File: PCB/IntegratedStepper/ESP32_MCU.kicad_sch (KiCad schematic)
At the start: 23 parts, among them Q1 SS8050-G, Q2 SS8050-G, U1 ESP32-WROOM-32E, U3 CP2102N-Axx-xQFN28

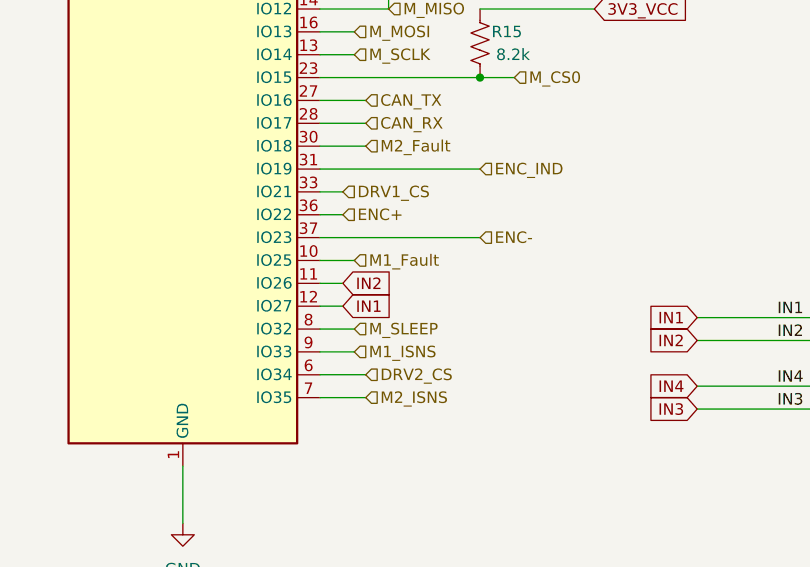
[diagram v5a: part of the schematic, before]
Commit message: update new layout with DRV8245
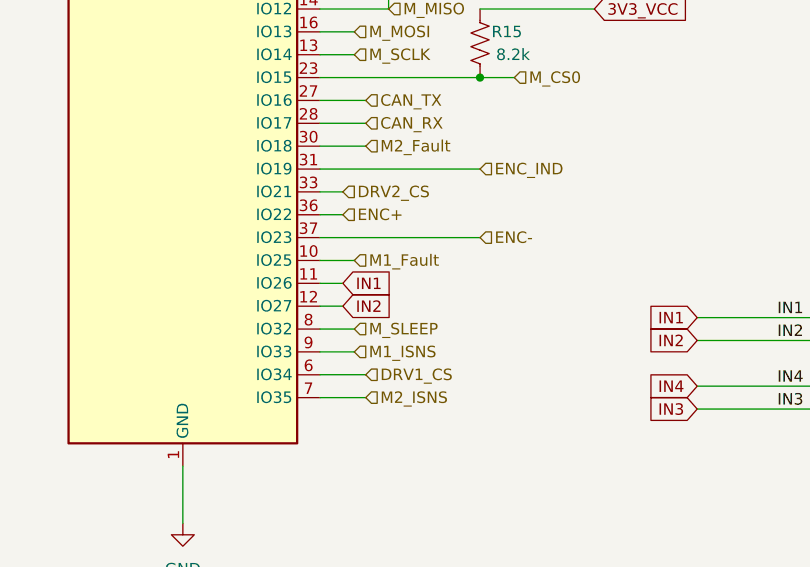
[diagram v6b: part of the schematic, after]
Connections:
- net DRV1_CS: now also U1.6 (IO34); no longer U1.33 (IO21)
- net DRV2_CS: now also U1.33 (IO21); no longer U1.6 (IO34)
- net IN1: now also U1.11 (IO26); no longer U1.12 (IO27)
- net IN2: now also U1.12 (IO27); no longer U1.11 (IO26)
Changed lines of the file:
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@@
+		)
+	)
+	(global_label "IN2"
+		(shape input)
+		(at 134.62 102.87 0)
+		(fields_autoplaced yes)
+		(effects
+			(font
+				(size 1.27 1.27)
+			)
+			(justify left)
+		)
+		(property "Intersheetrefs" "${INTERSHEET_REFS}"
+			(at 140.75 102.87 0)
+			(effects
+				(font
+					(size 1.27 1.27)
+				)
+				(justify left)
+				(hide yes)
+			)
 		)
 	)
@@
 		)
 	)
+	(global_label "IN1"
+		(shape input)
+		(at 134.62 100.33 0)
+		(fields_autoplaced yes)
+		(effects
+			(font
+				(size 1.27 1.27)
+			)
+			(justify left)
+		)
+		(property "Intersheetrefs" "${INTERSHEET_REFS}"
+			(at 140.75 100.33 0)
+			(effects
+				(font
+					(size 1.27 1.27)
+				)
+				(justify left)
+				(hide yes)
+			)
+		)
+	)
 	(global_label "EN"
 		(shape input)
@@
 		)
 	)
+	(global_label "RX"
+		(shape input)
+		(at 135.89 62.23 0)
+		(fields_autoplaced yes)
+		(effects
+			(font
+				(size 1.27 1.27)
+			)
+			(justify left)
+		)
+		(property "Intersheetrefs" "${INTERSHEET_REFS}"
+			(at 141.3547 62.23 0)
+			(effects
+				(font
+					(size 1.27 1.27)
+				)
+				(justify left)
+				(hide yes)
+			)
+		)
+	)
+	(global_label "DTR"
+		(shape input)
+		(at 36.83 147.32 180)
+		(fields_autoplaced yes)
+		(effects
+			(font
+				(size 1.27 1.27)
+			)
+			(justify right)
+		)
+		(property "Intersheetrefs" "${INTERSHEET_REFS}"
+			(at 30.3372 147.32 0)
+			(effects
+				(font
+					(size 1.27 1.27)
+				)
+				(justify right)
+				(hide yes)
+			)
+		)
+	)
+	(global_label "IN3"
+		(shape input)
+		(at 173.99 114.3 180)
+		(fields_autoplaced yes)
+		(effects
+			(font
+				(size 1.27 1.27)
+			)
+			(justify right)
+		)
+		(property "Intersheetrefs" "${INTERSHEET_REFS}"
+			(at 167.86 114.3 0)
+			(effects
+				(font
+					(size 1.27 1.27)
+				)
+				(justify right)
+				(hide yes)
+			)
+		)
+	)
 	(global_label "IN1"
 		(shape input)
-		(at 134.62 102.87 0)
-		(fields_autoplaced yes)
-		(effects
-			(font
-				(size 1.27 1.27)
-			)
-			(justify left)
-		)
-		(property "Intersheetrefs" "${INTERSHEET_REFS}"
-			(at 140.75 102.87 0)
-			(effects
-				(font
-					(size 1.27 1.27)
-				)
-				(justify left)
-				(hide yes)
-			)
-		)
-	)
-	(global_label "RX"
-		(shape input)
-		(at 135.89 62.23 0)
-		(fields_autoplaced yes)
-		(effects
-			(font
-				(size 1.27 1.27)
-			)
-			(justify left)
-		)
-		(property "Intersheetrefs" "${INTERSHEET_REFS}"
-			(at 141.3547 62.23 0)
-			(effects
-				(font
-					(size 1.27 1.27)
-				)
-				(justify left)
-				(hide yes)
-			)
-		)
-	)
-	(global_label "DTR"
-		(shape input)
-		(at 36.83 147.32 180)
-		(fields_autoplaced yes)
-		(effects
-			(font
-				(size 1.27 1.27)
-			)
-			(justify right)
-		)
-		(property "Intersheetrefs" "${INTERSHEET_REFS}"
-			(at 30.3372 147.32 0)
-			(effects
-				(font
-					(size 1.27 1.27)
-				)
-				(justify right)
-				(hide yes)
-			)
-		)
-	)
-	(global_label "IN3"
-		(shape input)
-		(at 173.99 114.3 180)
-		(fields_autoplaced yes)
-		(effects
-			(font
-				(size 1.27 1.27)
-			)
-			(justify right)
-		)
-		(property "Intersheetrefs" "${INTERSHEET_REFS}"
-			(at 167.86 114.3 0)
-			(effects
-				(font
-					(size 1.27 1.27)
-				)
-				(justify right)
-				(hide yes)
-			)
-		)
-	)
-	(global_label "IN1"
-		(shape input)
 		(at 173.99 104.14 180)
 		(fields_autoplaced yes)
@@
 		)
 	)
-	(global_label "IN2"
-		(shape input)
-		(at 134.62 100.33 0)
-		(fields_autoplaced yes)
-		(effects
-			(font
-				(size 1.27 1.27)
-			)
-			(justify left)
-		)
-		(property "Intersheetrefs" "${INTERSHEET_REFS}"
-			(at 140.75 100.33 0)
-			(effects
-				(font
-					(size 1.27 1.27)
-				)
-				(justify left)
-				(hide yes)
-			)
-		)
-	)
 	(global_label "IN4"
 		(shape input)
@@
 		)
 	)
+	(hierarchical_label "DRV1_CS"
+		(shape input)
+		(at 137.16 110.49 0)
+		(fields_autoplaced yes)
+		(effects
+			(font
+				(size 1.27 1.27)
+			)
+			(justify left)
+		)
+	)
+	(hierarchical_label "DRV2_CS"
+		(shape input)
+		(at 134.62 90.17 0)
+		(fields_autoplaced yes)
+		(effects
+			(font
+				(size 1.27 1.27)
+			)
+			(justify left)
+		)
+	)
 	(hierarchical_label "CAN_TX"
 		(shape input)
@@
 		)
 	)
-	(hierarchical_label "DRV2_CS"
-		(shape input)
-		(at 137.16 110.49 0)
-		(fields_autoplaced yes)
-		(effects
-			(font
-				(size 1.27 1.27)
-			)
-			(justify left)
-		)
-	)
 	(hierarchical_label "M1_Fault"
 		(shape input)
@@
 		)
 	)
-	(hierarchical_label "DRV1_CS"
-		(shape input)
-		(at 134.62 90.17 0)
-		(fields_autoplaced yes)
-		(effects
-			(font
-				(size 1.27 1.27)
-			)
-			(justify left)
-		)
-	)

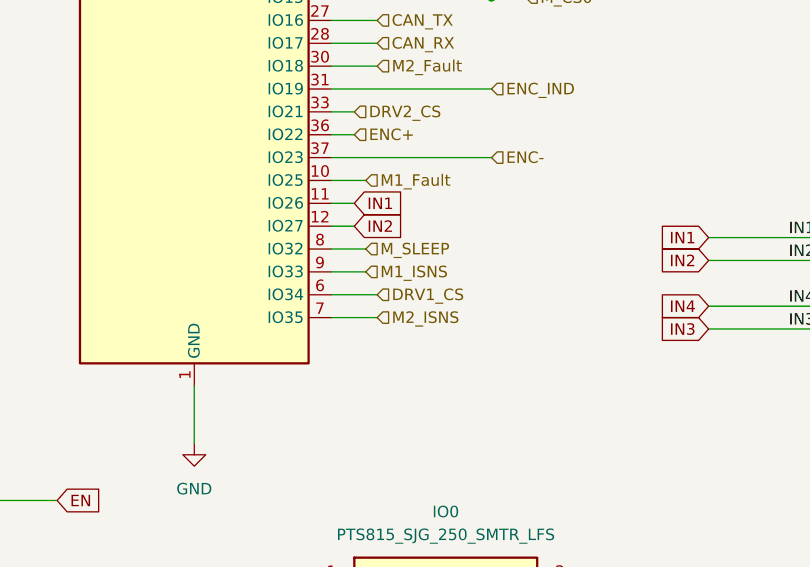
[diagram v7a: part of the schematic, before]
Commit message: update pinout for ESP32
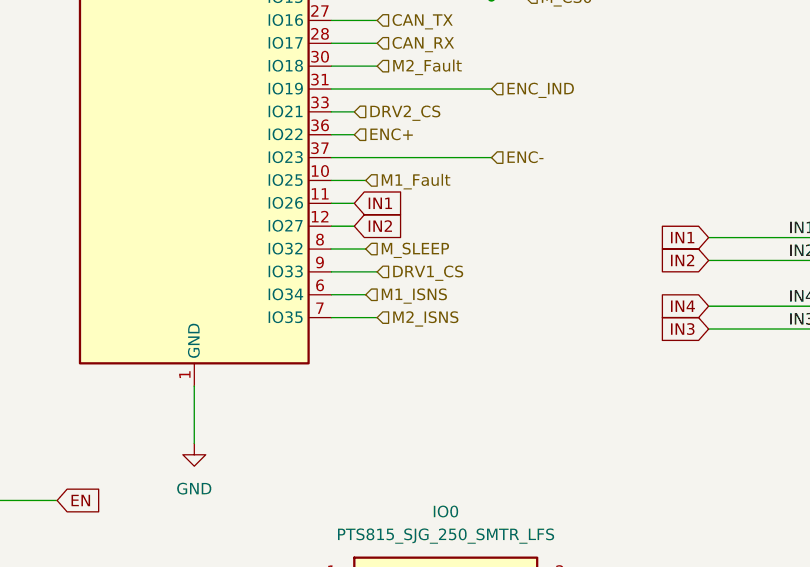
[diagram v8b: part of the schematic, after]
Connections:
- net DRV1_CS: now also U1.9 (IO33); no longer U1.6 (IO34)
- net M1_ISNS: now also U1.6 (IO34); no longer U1.9 (IO33)
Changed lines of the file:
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@@
-	(wire
-		(pts
-			(xy 132.08 107.95) (xy 135.89 107.95)
-		)
-		(stroke
-			(width 0)
-			(type default)
-		)
-	)
 	(wire
 		(pts
@@
 	(wire
 		(pts
-			(xy 132.08 110.49) (xy 137.16 110.49)
+			(xy 132.08 110.49) (xy 135.89 110.49)
 		)
 		(stroke
@@
 		(pts
 			(xy 173.99 106.68) (xy 186.69 106.68)
+		)
+		(stroke
+			(width 0)
+			(type default)
+		)
+	)
+	(wire
+		(pts
+			(xy 132.08 107.95) (xy 137.16 107.95)
 		)
 		(stroke
@@
 	(hierarchical_label "DRV1_CS"
 		(shape input)
-		(at 137.16 110.49 0)
+		(at 137.16 107.95 0)
 		(fields_autoplaced yes)
 		(effects
@@
 		)
 	)
+	(hierarchical_label "M2_ISNS"
+		(shape input)
+		(at 137.16 113.03 0)
+		(fields_autoplaced yes)
+		(effects
+			(font
+				(size 1.27 1.27)
+			)
+			(justify left)
+		)
+	)
+	(hierarchical_label "M1_Fault"
+		(shape input)
+		(at 135.89 97.79 0)
+		(fields_autoplaced yes)
+		(effects
+			(font
+				(size 1.27 1.27)
+			)
+			(justify left)
+		)
+	)
+	(hierarchical_label "ENC_IND"
+		(shape input)
+		(at 149.86 87.63 0)
+		(fields_autoplaced yes)
+		(effects
+			(font
+				(size 1.27 1.27)
+			)
+			(justify left)
+		)
+	)
+	(hierarchical_label "USB_D+"
+		(shape input)
+		(at 203.2 71.12 180)
+		(fields_autoplaced yes)
+		(effects
+			(font
+				(size 1.27 1.27)
+			)
+			(justify right)
+		)
+	)
+	(hierarchical_label "M_SLEEP"
+		(shape input)
+		(at 135.89 105.41 0)
+		(fields_autoplaced yes)
+		(effects
+			(font
+				(size 1.27 1.27)
+			)
+			(justify left)
+		)
+	)
+	(hierarchical_label "IN[1..4]"
+		(shape input)
+		(at 191.77 101.6 0)
+		(fields_autoplaced yes)
+		(effects
+			(font
+				(size 1.27 1.27)
+			)
+			(justify left)
+		)
+	)
+	(hierarchical_label "3V3_VCC"
+		(shape input)
+		(at 229.87 39.37 0)
+		(fields_autoplaced yes)
+		(effects
+			(font
+				(size 1.27 1.27)
+			)
+			(justify left)
+		)
+	)
+	(hierarchical_label "ENC-"
+		(shape input)
+		(at 149.86 95.25 0)
+		(fields_autoplaced yes)
+		(effects
+			(font
+				(size 1.27 1.27)
+			)
+			(justify left)
+		)
+	)
 	(hierarchical_label "M1_ISNS"
 		(shape input)
-		(at 135.89 107.95 0)
-		(fields_autoplaced yes)
-		(effects
-			(font
-				(size 1.27 1.27)
-			)
-			(justify left)
-		)
-	)
-	(hierarchical_label "M2_ISNS"
-		(shape input)
-		(at 137.16 113.03 0)
-		(fields_autoplaced yes)
-		(effects
-			(font
-				(size 1.27 1.27)
-			)
-			(justify left)
-		)
-	)
-	(hierarchical_label "M1_Fault"
-		(shape input)
-		(at 135.89 97.79 0)
-		(fields_autoplaced yes)
-		(effects
-			(font
-				(size 1.27 1.27)
-			)
-			(justify left)
-		)
-	)
-	(hierarchical_label "ENC_IND"
-		(shape input)
-		(at 149.86 87.63 0)
-		(fields_autoplaced yes)
-		(effects
-			(font
-				(size 1.27 1.27)
-			)
-			(justify left)
-		)
-	)
-	(hierarchical_label "USB_D+"
-		(shape input)
-		(at 203.2 71.12 180)
-		(fields_autoplaced yes)
-		(effects
-			(font
-				(size 1.27 1.27)
-			)
-			(justify right)
-		)
-	)
-	(hierarchical_label "M_SLEEP"
-		(shape input)
-		(at 135.89 105.41 0)
-		(fields_autoplaced yes)
-		(effects
-			(font
-				(size 1.27 1.27)
-			)
-			(justify left)
-		)
-	)
-	(hierarchical_label "IN[1..4]"
-		(shape input)
-		(at 191.77 101.6 0)
-		(fields_autoplaced yes)
-		(effects
-			(font
-				(size 1.27 1.27)
-			)
-			(justify left)
-		)
-	)
-	(hierarchical_label "3V3_VCC"
-		(shape input)
-		(at 229.87 39.37 0)
-		(fields_autoplaced yes)
-		(effects
-			(font
-				(size 1.27 1.27)
-			)
-			(justify left)
-		)
-	)
-	(hierarchical_label "ENC-"
-		(shape input)
-		(at 149.86 95.25 0)
-		(fields_autoplaced yes)
-		(effects
+		(at 135.89 110.49 0)
+		(fields_autoplaced yes)
+		(effects
